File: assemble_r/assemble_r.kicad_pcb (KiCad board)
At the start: 2 copper layers, 128.5 x 92.1 mm, 45 parts, among them J23 Conn_01x02_Pin, SW23 SW_Push, SW24 SW_Push, SW25 SW_Push, SW26 SW_Push, SW27 SW_Push, SW28 SW_Push, SW29 SW_Push, SW30 SW_Push, SW31 SW_Push, SW32 SW_Push, SW33 SW_Push, SW34 SW_Push, SW35 SW_Push, SW36 SW_Push, SW37 SW_Push, SW38 SW_Push, SW39 SW_Push, SW40 SW_Push, SW41 SW_Push, SW42 SW_Push, SW43 SW_Push, SW44 SW_Push, U23 Micon_BLEMicroPro

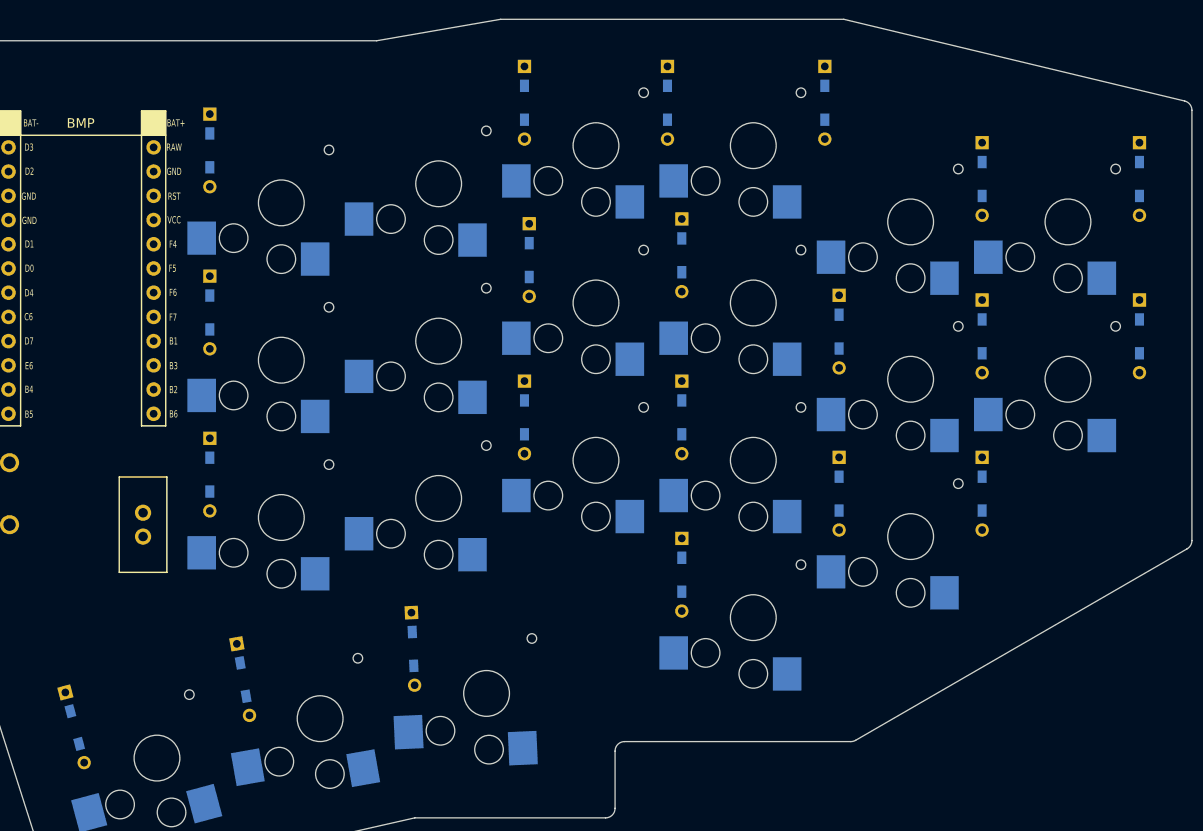
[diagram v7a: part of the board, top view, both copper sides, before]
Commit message: fix: place of diode
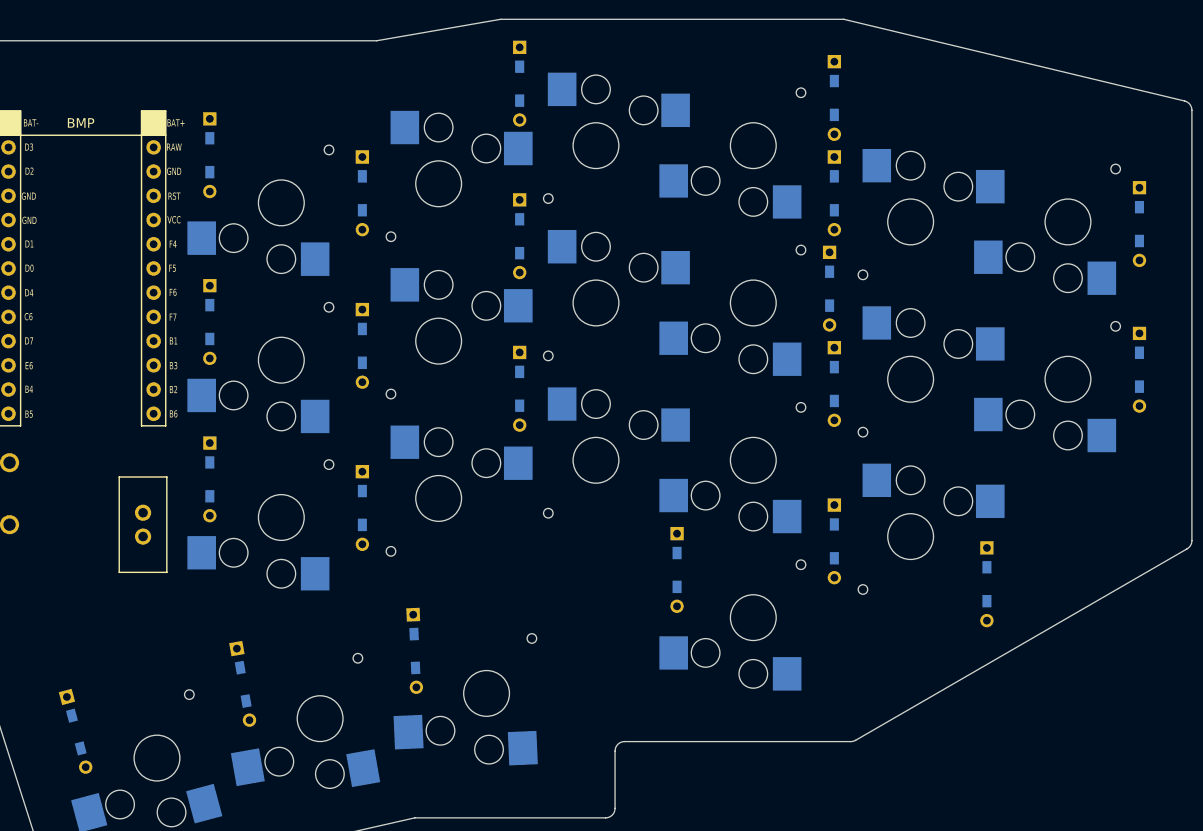
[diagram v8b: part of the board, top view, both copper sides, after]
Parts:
- moved D28 19.7 mm to (79.5, 64.0)
- moved D27 19.5 mm to (79.5, 48.0)
- moved D29 19.5 mm to (79.5, 81.0)
- moved D33 17.3 mm to (96.0, 68.5)
- moved D32 17.1 mm to (96.0, 52.5)
- moved D40 16.3 mm to (129.0, 68.0)
- moved D31 15.6 mm to (96.0, 36.5)
- moved D39 15.6 mm to (129.0, 48.0)
- moved D41 9.51 mm to (145.0, 89.0)
- moved D37 5.02 mm to (129.0, 84.5)
- moved D42 4.73 mm to (161.0, 51.2)
- moved D36 4.61 mm to (128.5, 58.0)
- moved D43 3.50 mm to (161.0, 66.5)
- moved D35 1.12 mm to (129.0, 38.0)
- moved D24 1.00 mm to (63.5, 61.5)
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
